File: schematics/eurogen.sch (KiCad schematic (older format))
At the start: 22 parts, among them J1 PJ301M-12, J3 PJ301M-12, J4 EURO_PWR_2x5, U1 ESP32-DEVKITC-32D, U2 CODECODER-WM8731SEDS_V(SSOP28), U3 MCP3208

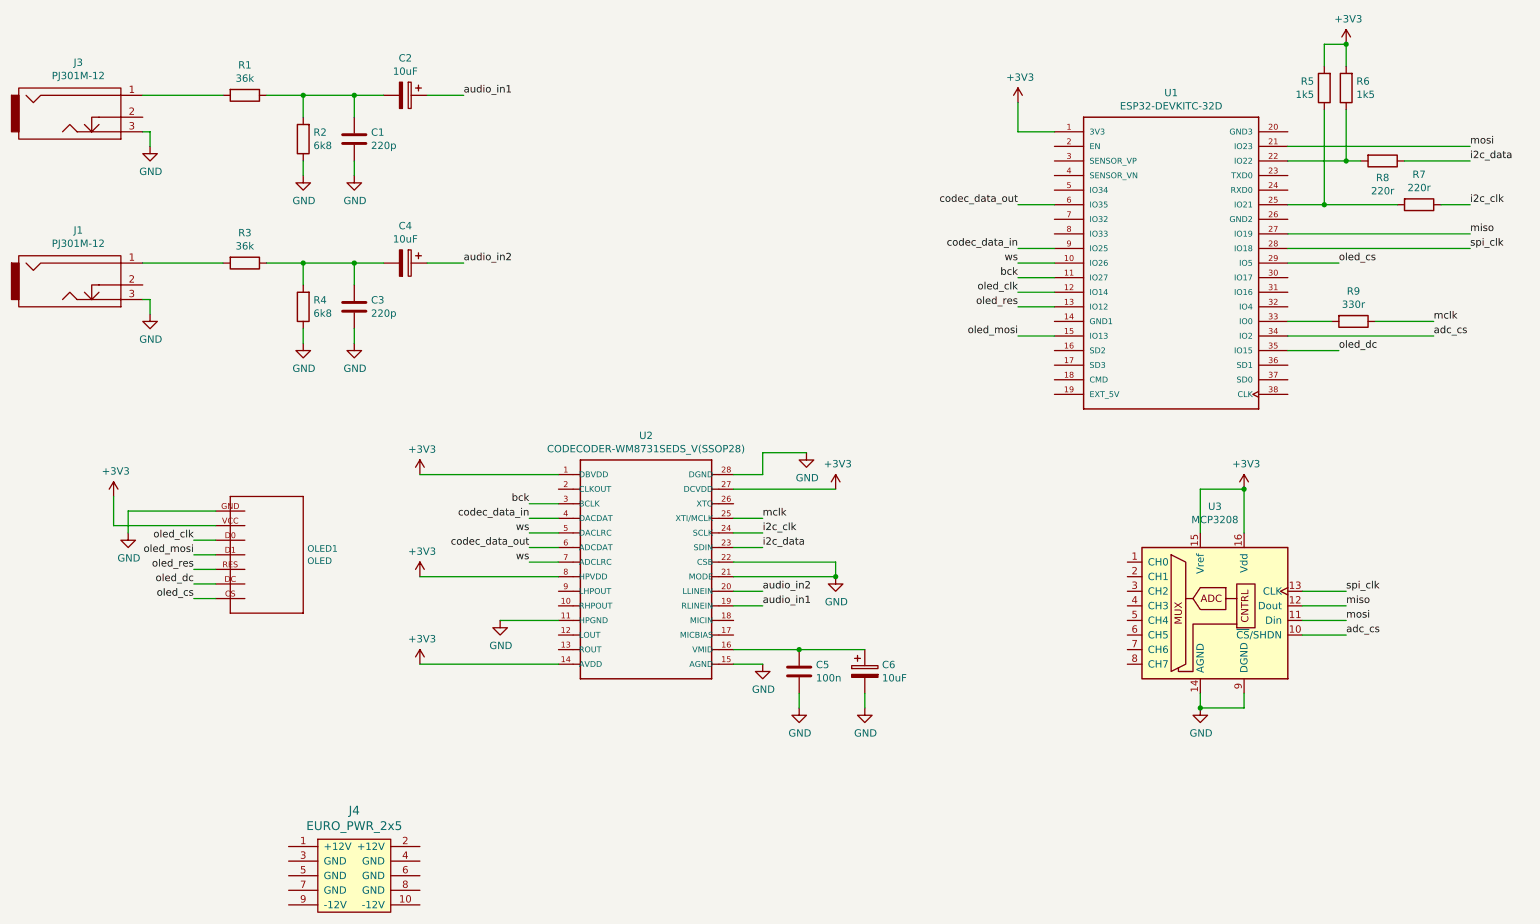
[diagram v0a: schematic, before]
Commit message: added rotary encoder. schematics PDF
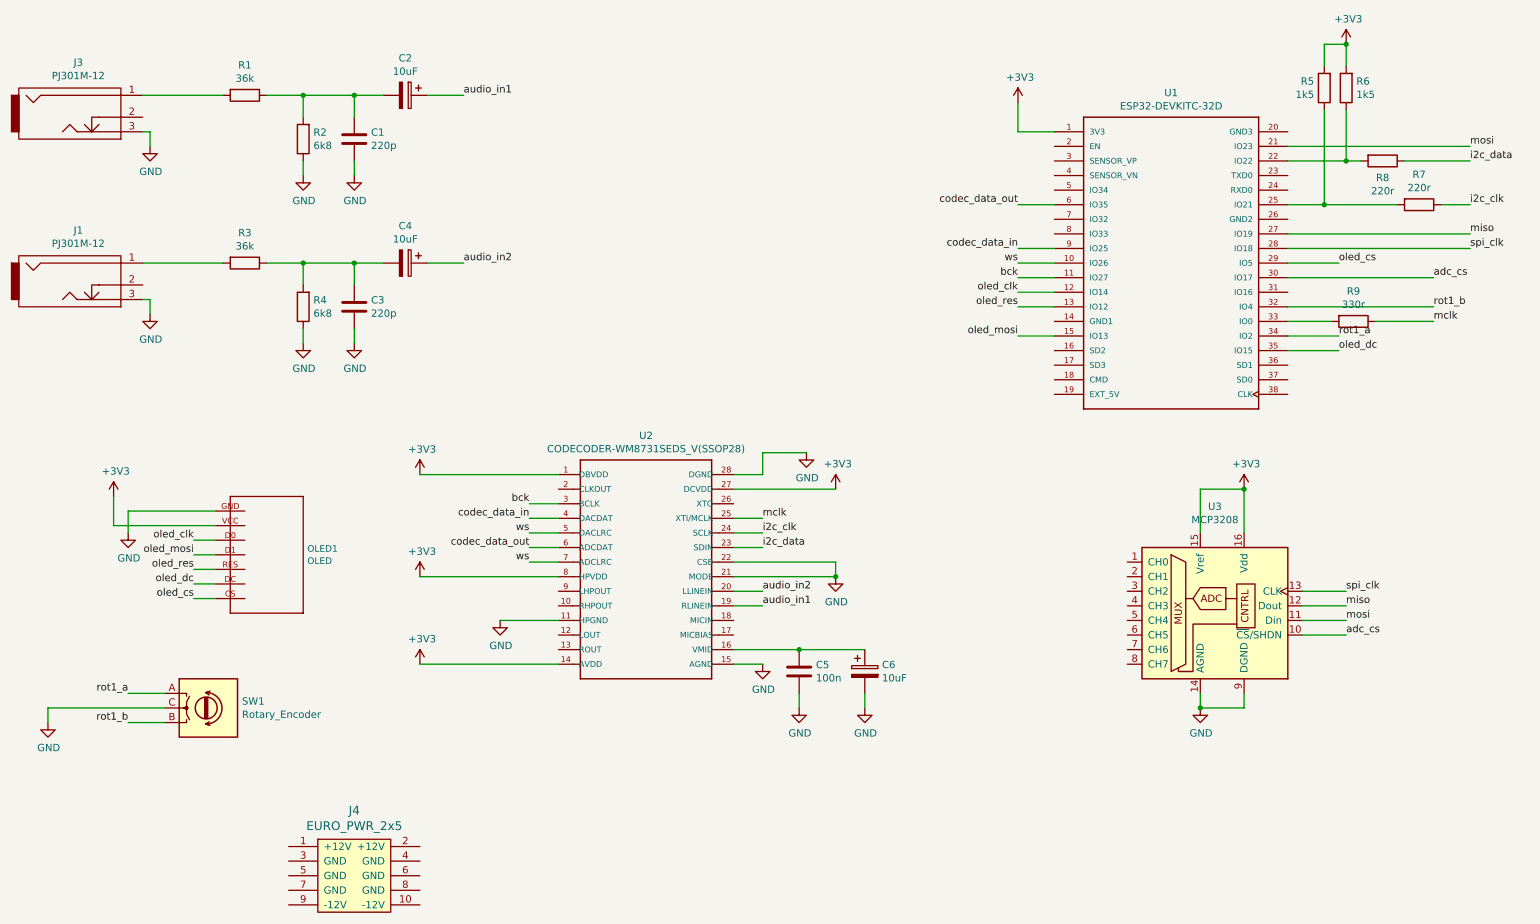
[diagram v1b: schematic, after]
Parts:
- added SW1: Rotary_Encoder, symbol Device:Rotary_Encoder
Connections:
- net GND: now also SW1.C
- net adc_cs: now also U1.30 (IO17); no longer U1.34 (IO2)
- net rot1_b: now reaches U1.32 (IO4)
- net rot1_b: now also SW1.B
- new net rot1_a: SW1.A, U1.34 (IO2)
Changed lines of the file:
@@
 Wire Wire Line
 	9950 4700 9650 4700
-Text Label 10550 2750 0    50   ~ 0
+Text Label 10550 2350 0    50   ~ 0
 adc_cs
-Wire Wire Line
-	10550 2750 9550 2750
 Wire Wire Line
 	9550 1550 9950 1550
@@
 Wire Wire Line
 	9900 2250 9550 2250
+$Comp
+L Device:Rotary_Encoder SW1
+U 1 1 5E5B9F74
+P 2150 5300
+F 0 "SW1" H 2380 5346 50  0000 L CNN
+F 1 "Rotary_Encoder" H 2380 5255 50  0000 L CNN
+F 2 "" H 2000 5460 50  0001 C CNN
+F 3 "~" H 2150 5560 50  0001 C CNN
+	1    2150 5300
+	1    0    0    -1
+$EndComp
+$Comp
+L power:GND #PWR022
+U 1 1 5E5BCC80
+P 1050 5400
+F 0 "#PWR022" H 1050 5150 50  0001 C CNN
+F 1 "GND" H 1055 5227 50  0000 C CNN
+F 2 "" H 1050 5400 50  0001 C CNN
+F 3 "" H 1050 5400 50  0001 C CNN
+	1    1050 5400
+	1    0    0    -1
+$EndComp
+Wire Wire Line
+	1850 5300 1050 5300
+Wire Wire Line
+	1050 5300 1050 5400
+Text Label 1600 5200 2    50   ~ 0
+rot1_a
+Text Label 1600 5400 2    50   ~ 0
+rot1_b
+Wire Wire Line
+	1600 5400 1850 5400
+Wire Wire Line
+	1850 5200 1600 5200
+Wire Wire Line
+	9550 2350 10550 2350
+Text Label 9900 2750 0    50   ~ 0
+rot1_a
+Wire Wire Line
+	9900 2750 9550 2750
+Text Label 10550 2550 0    50   ~ 0
+rot1_b
+Wire Wire Line
+	10550 2550 9550 2550
 $EndSCHEMATC
